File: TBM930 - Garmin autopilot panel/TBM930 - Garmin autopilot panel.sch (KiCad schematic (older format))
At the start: 28 parts, among them J10 AVR-ISP-6, J11 Screw_Terminal_01x02, J8 Barrel_Jack, J9 USB_B_Mini, SW2 SW_Push

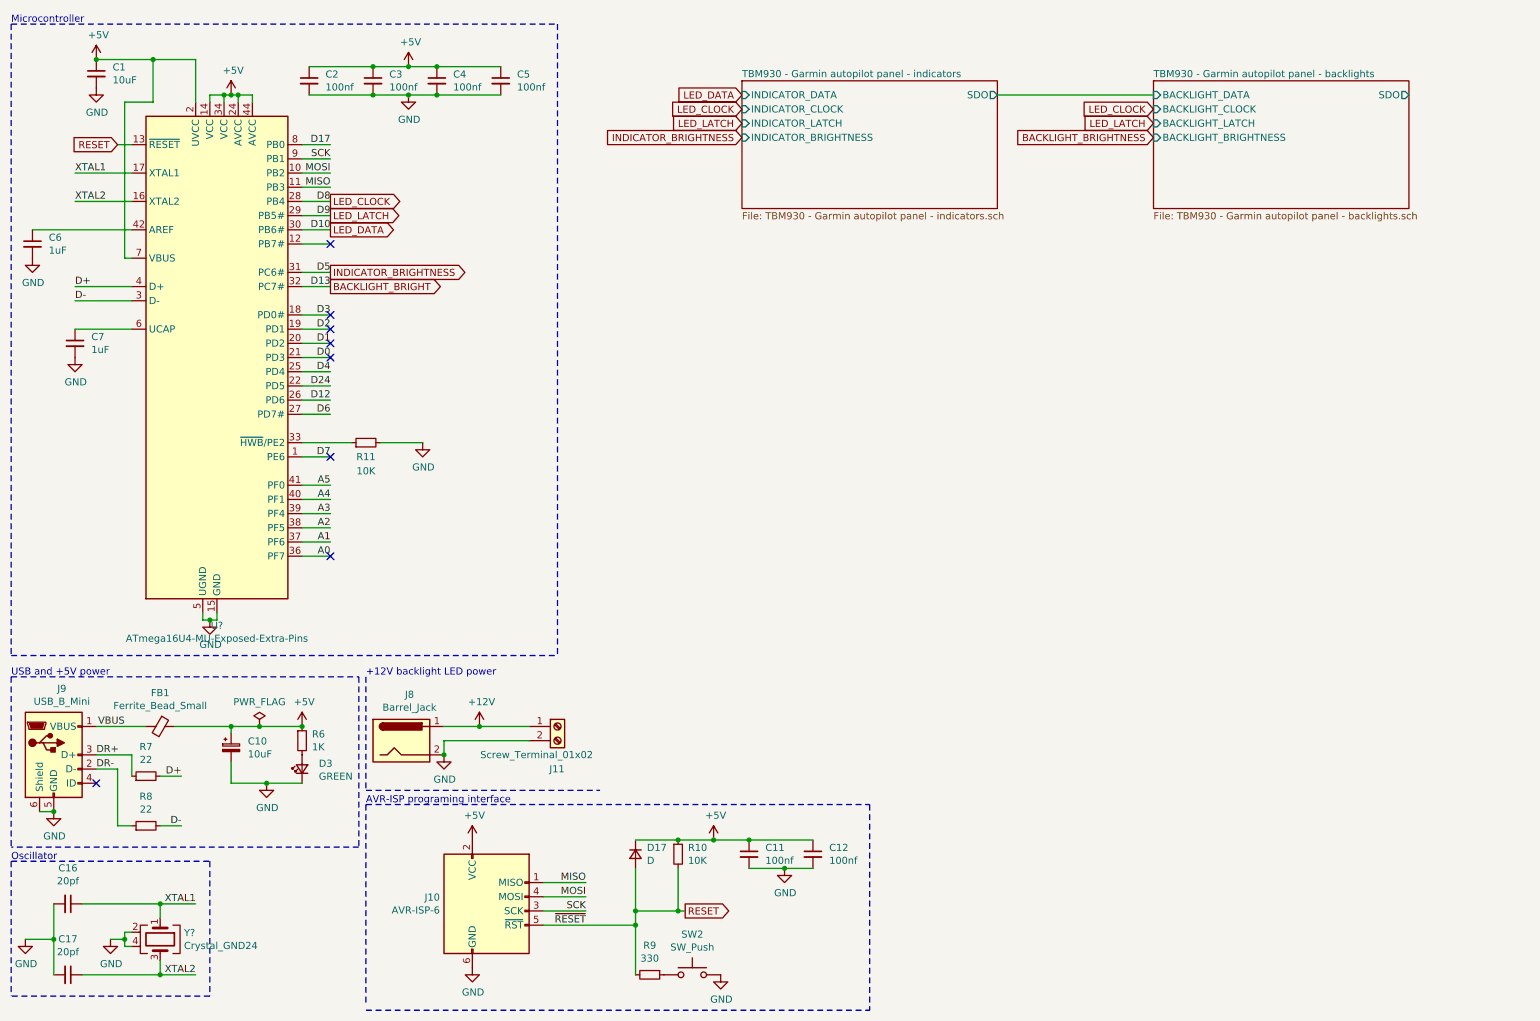
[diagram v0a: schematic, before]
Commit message: Add all the inputs
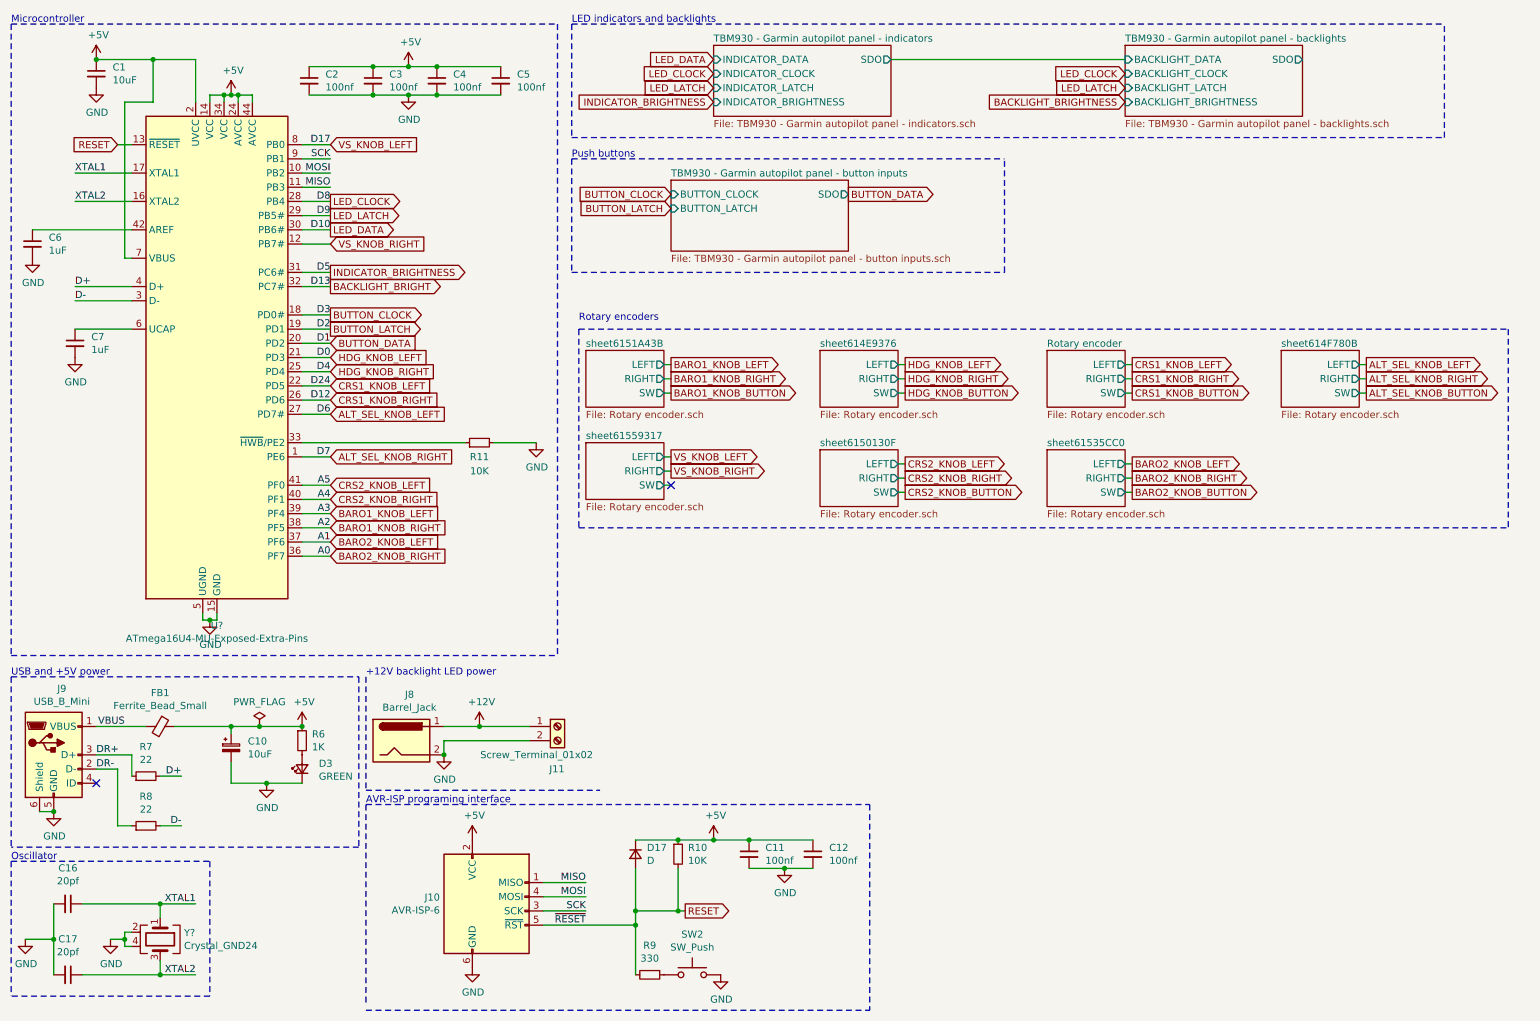
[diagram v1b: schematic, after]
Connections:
- net VS_KNOB_RIGHT: now reaches U?.12 (PB7#)
- net A0 renamed BARO2_KNOB_RIGHT
- net A1 renamed BARO2_KNOB_LEFT
- net A2 renamed BARO1_KNOB_RIGHT
- net A3 renamed BARO1_KNOB_LEFT
- net A4 renamed CRS2_KNOB_RIGHT
- net A5 renamed CRS2_KNOB_LEFT
- net D0 renamed HDG_KNOB_LEFT
- net D1 renamed BUTTON_DATA
- net D12 renamed CRS1_KNOB_RIGHT
- net D17 renamed VS_KNOB_LEFT
- net D2 renamed BUTTON_LATCH
- net D24 renamed CRS1_KNOB_LEFT
- net D3 renamed BUTTON_CLOCK
- net D4 renamed HDG_KNOB_RIGHT
- net D6 renamed ALT_SEL_KNOB_LEFT
- net D7 renamed ALT_SEL_KNOB_RIGHT
- no-connect marks 8 -> 2
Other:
- note added: "LED indicators and backlights"
- note added: "Push buttons"
- note added: "Rotary encoders"
- moved on the sheet: R11

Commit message: More AP updates
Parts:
- added U?: AMS1117-5.0, Package_TO_SOT_SMD:SOT-223-3_TabPin2, symbol Regulator_Linear:AMS1117-5.0
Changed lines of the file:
@@
 Text GLabel 2750 2150 2    50   Input ~ 0
 VS_KNOB_RIGHT
+$Comp
+L Regulator_Linear:AMS1117-5.0 U?
+U 1 1 613DD700
+P 5150 5600
+F 0 "U?" H 5150 5842 50  0000 C CNN
+F 1 "AMS1117-5.0" H 5150 5751 50  0000 C CNN
+F 2 "Package_TO_SOT_SMD:SOT-223-3_TabPin2" H 5150 5800 50  0001 C CNN
+F 3 "http://www.advanced-monolithic.com/pdf/ds1117.pdf" H 5250 5350 50  0001 C CNN
+	1    5150 5600
+	1    0    0    -1
+$EndComp
 $EndSCHEMATC
